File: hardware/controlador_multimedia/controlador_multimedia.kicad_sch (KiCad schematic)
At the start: 10 parts, among them J1 Conn_01x15, J2 Conn_01x15, SW1 SW_Push, SW2 SW_Push, SW3 SW_Push, SW4 RotaryEncoder_Switch

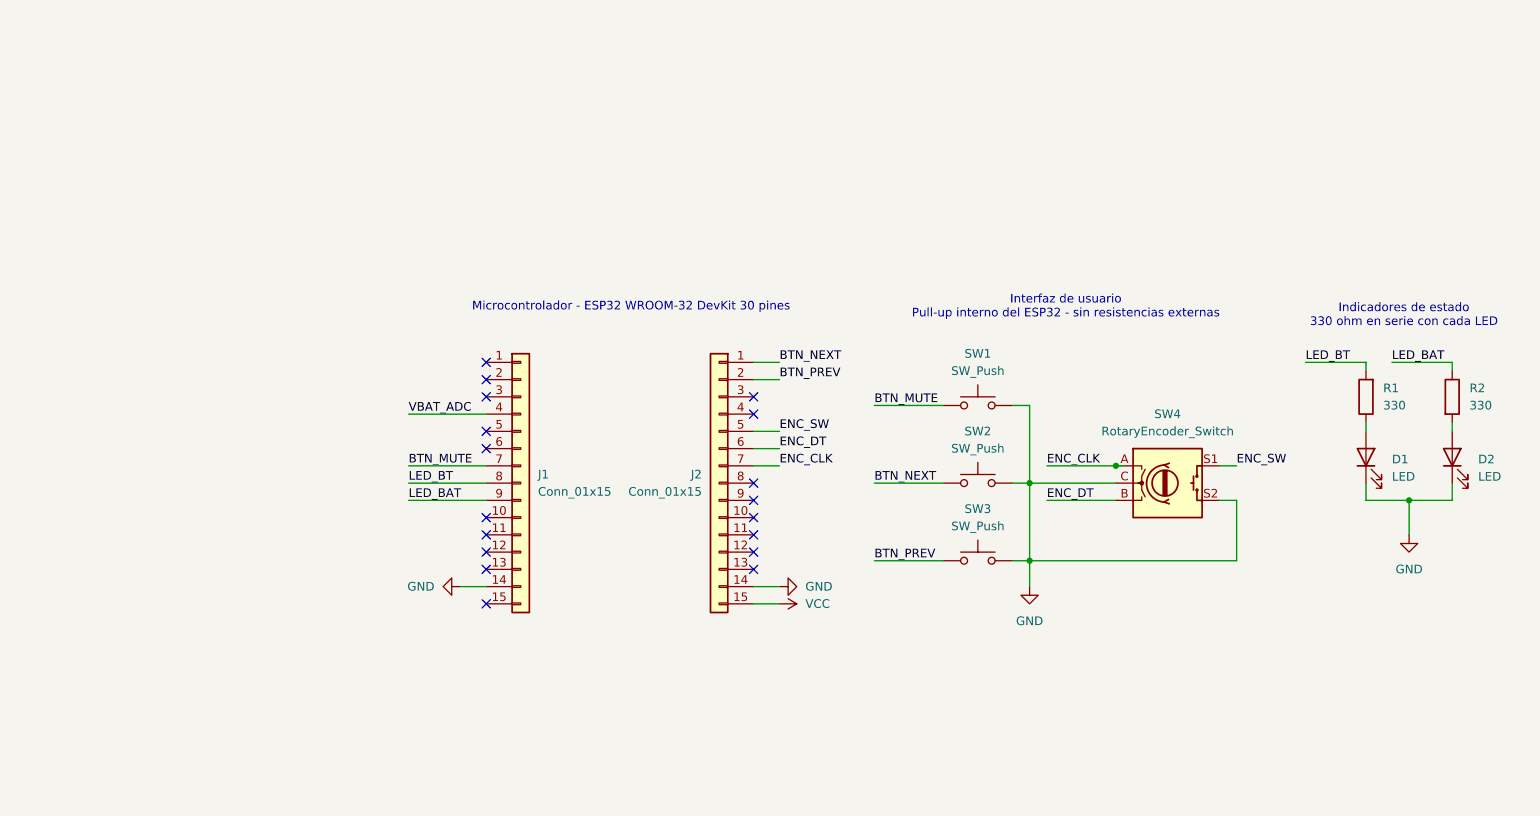
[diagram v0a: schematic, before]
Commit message: hardware: completar esquemático con cadena de potencia y ERC sin errores
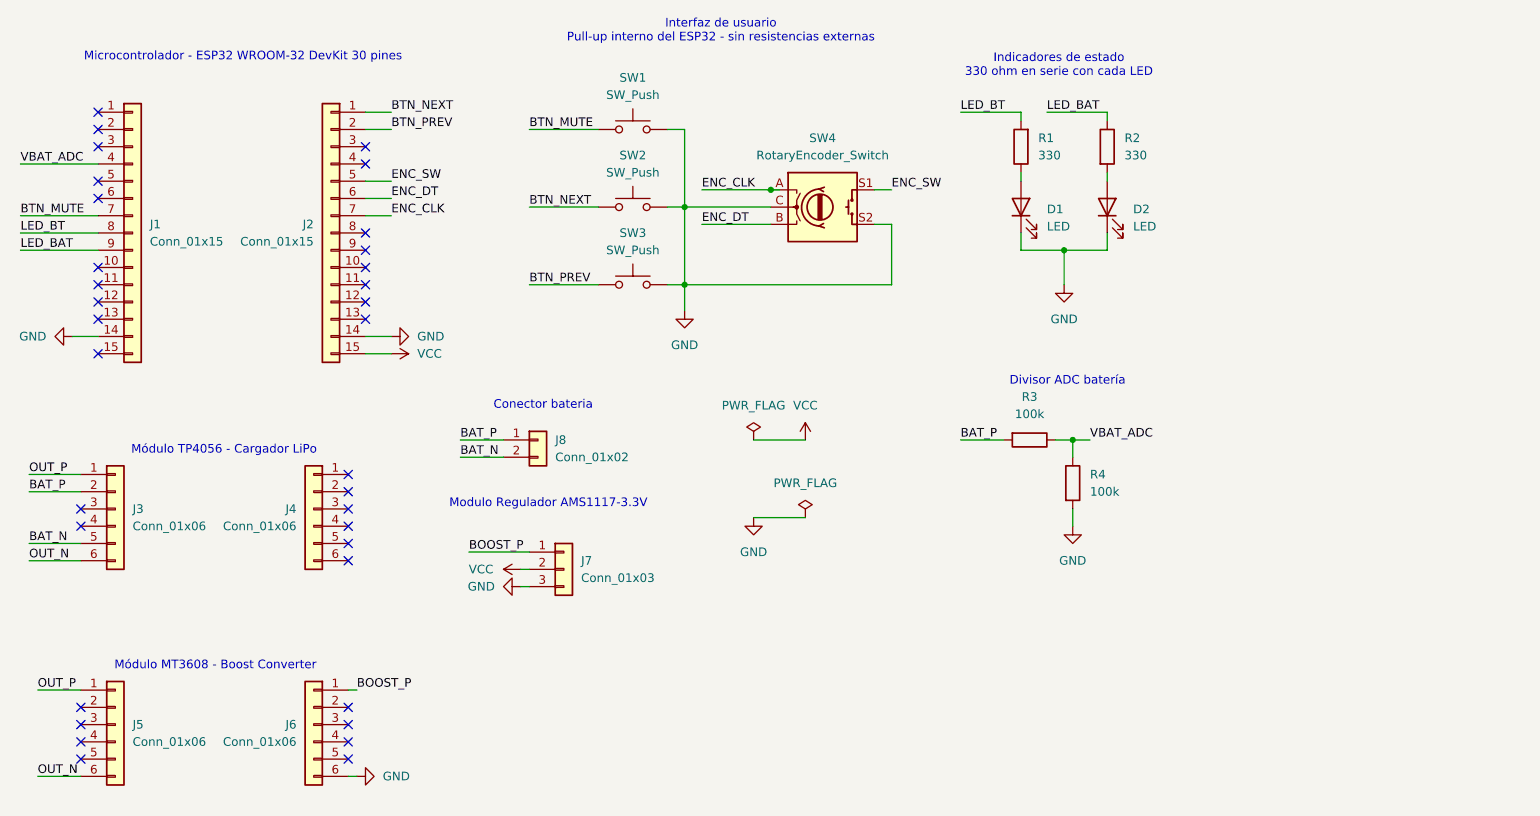
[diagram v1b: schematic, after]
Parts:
- added J3, J4, J5, J6: Conn_01x06, symbol Connector_Generic:Conn_01x06
- added J7: Conn_01x03, symbol Connector_Generic:Conn_01x03
- added J8: Conn_01x02, symbol Connector_Generic:Conn_01x02
- added R3, R4: 100k, symbol Device:R
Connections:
- net GND: now also J6.6 (Pin_6), J7.3 (Pin_3), R4.2
- net VBAT_ADC: now also R3.1, R4.1
- net VCC: now also J7.2 (Pin_2)
- new net BAT_N: J3.5 (Pin_5), J8.2 (Pin_2)
- new net BAT_P: J3.2 (Pin_2), J8.1 (Pin_1), R3.2
- new net BOOST_P: J6.1 (Pin_1), J7.1 (Pin_1)
- new net OUT_N: J3.6 (Pin_6), J5.6 (Pin_6)
- new net OUT_P: J3.1 (Pin_1), J5.1 (Pin_1)
- no-connect marks 18 -> 34
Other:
- note added: "Conector bateria"
- note added: "Divisor ADC batería"
- note added: "Modulo Regulador AMS1117-3.3V"
- note added: "Módulo MT3608 - Boost Converter"
- note added: "Módulo TP4056 - Cargador LiPo"
- company: (none) -> Mario Alberto Nina Gallo
- moved on the sheet: D1, D2, J1, J2, R1, R2, SW1, SW2, SW3, SW4

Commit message: hardware: asignar huellas y modelos 3D a todos los componentes
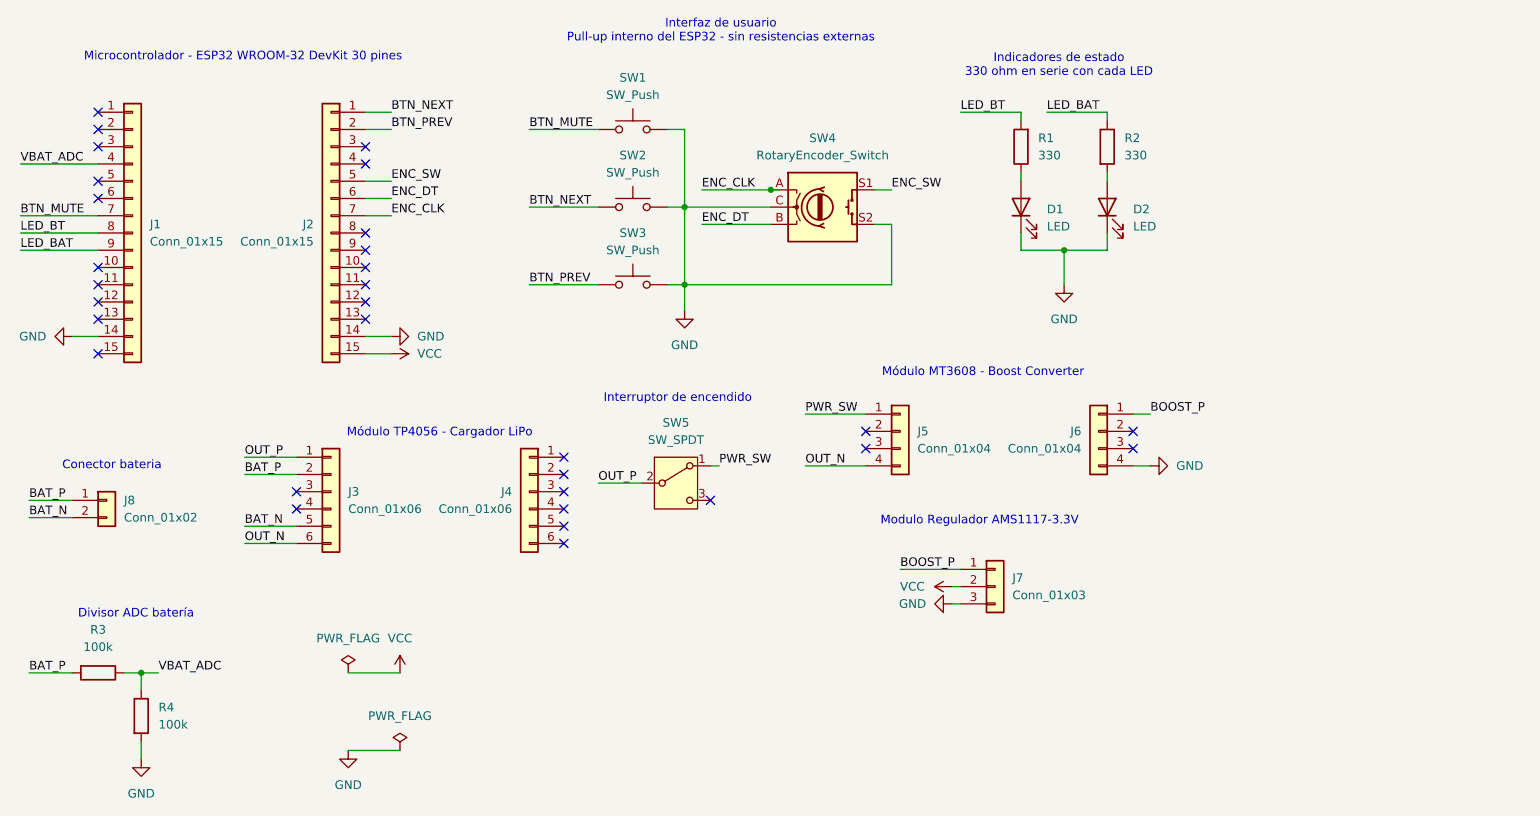
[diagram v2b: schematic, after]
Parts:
- removed J5, J6: Conn_01x06, symbol Connector_Generic:Conn_01x06
- added J5, J6: Conn_01x04, Connector_PinHeader_2.54mm:PinHeader_1x04_P2.54mm_Vertical, symbol Connector_Generic:Conn_01x04
- added SW5: SW_SPDT, Custom:Schiebeschalter_SS-12D00, symbol Switch:SW_SPDT
- D1, D2: footprint (none) -> LED_THT:LED_D5.0mm
- J1, J2: footprint (none) -> Connector_PinSocket_2.54mm:PinSocket_1x15_P2.54mm_Vertical
- J3, J4: footprint (none) -> Connector_PinHeader_2.54mm:PinHeader_1x06_P2.54mm_Vertical
- J7: footprint (none) -> Connector_PinHeader_2.54mm:PinHeader_1x03_P2.54mm_Vertical
- J8: footprint (none) -> TerminalBlock_Phoenix:TerminalBlock_Phoenix_MKDS-1,5-2_1x02_P5.00mm_Horizontal
- R1, R2, R3, R4: footprint (none) -> Resistor_THT:R_Axial_DIN0207_L6.3mm_D2.5mm_P7.62mm_Horizontal
- SW1, SW2, SW3: footprint (none) -> Button_Switch_THT:SW_PUSH_6mm_H5mm
- SW4: footprint (none) -> Rotary_Encoder:RotaryEncoder_Alps_EC11E-Switch_Vertical_H20mm
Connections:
- net BOOST_P: now also J6.1 (Pin_1)
- net GND: now also J6.4 (Pin_4)
- net OUT_N: now also J5.4 (Pin_4)
- net OUT_P: now also SW5.2 (B)
- new net PWR_SW: J5.1 (Pin_1), SW5.1 (A)
- no-connect marks 34 -> 31
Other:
- note added: "Interruptor de encendido"
- moved on the sheet: J3, J4, J7, J8, R3, R4

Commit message: refactor: centralizar pines en common/pines.h
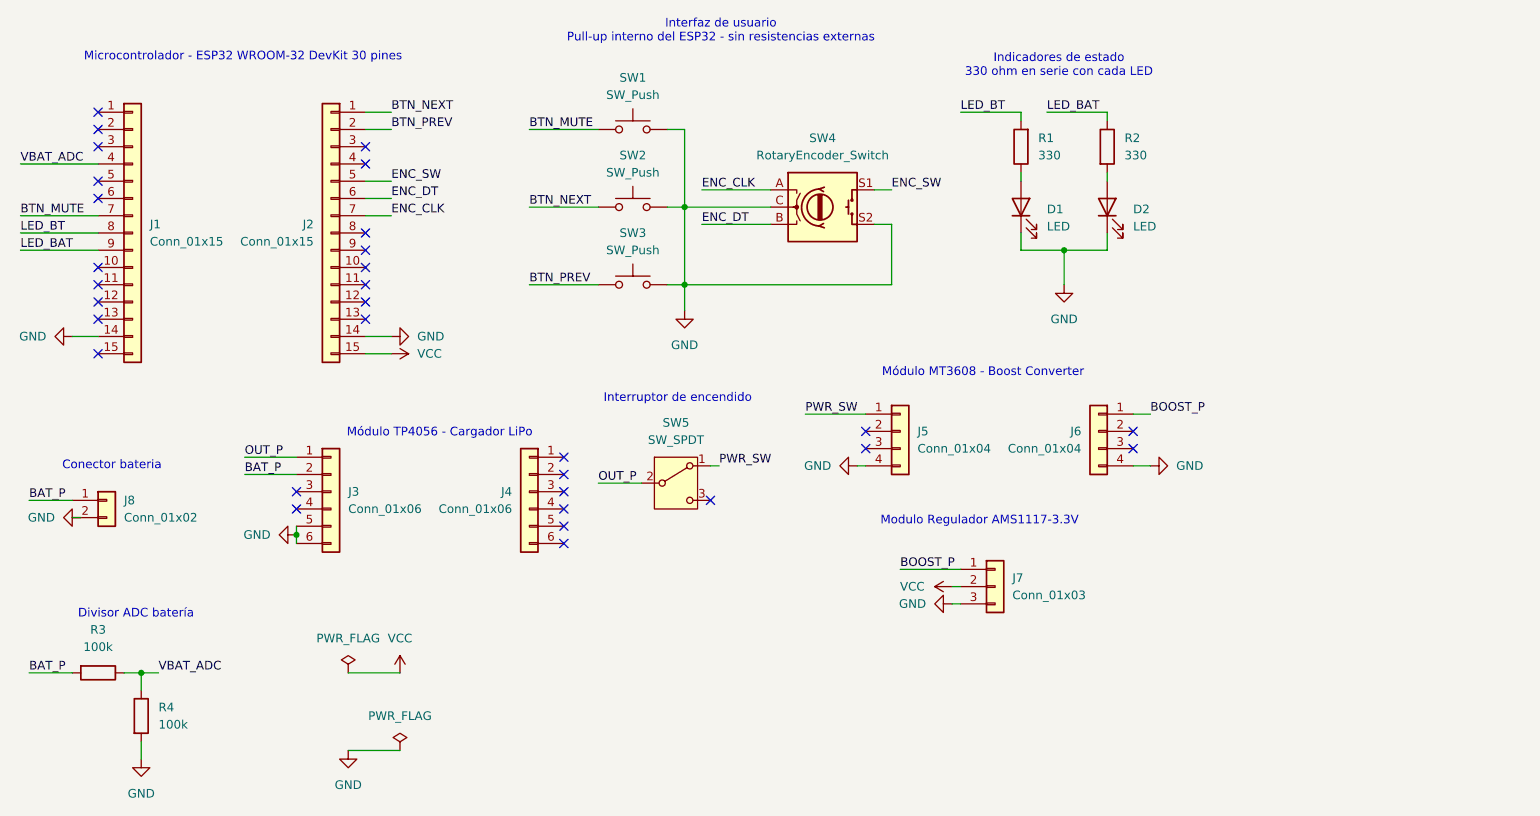
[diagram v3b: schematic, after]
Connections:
- net BAT_N is gone; now on net GND: J3.5 (Pin_5), J8.2 (Pin_2)
- net OUT_N is gone; now on net GND: J3.6 (Pin_6), J5.4 (Pin_4)
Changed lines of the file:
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@@
 	)
 	(junction
-		(at 35.56 110.49)
+		(at 58.42 90.17)
 		(diameter 0)
 		(color 0 0 0 0)
 	)
 	(junction
-		(at 128.27 39.37)
+		(at 35.56 110.49)
 		(diameter 0)
 		(color 0 0 0 0)
@@
 	(wire
 		(pts
-			(xy 50.8 88.9) (xy 58.42 88.9)
-		)
-		(stroke
-			(width 0)
-			(type default)
-		)
-	)
-	(wire
-		(pts
 			(xy 115.57 41.91) (xy 115.57 53.34)
 		)
@@
 	(wire
 		(pts
-			(xy 118.11 39.37) (xy 128.27 39.37)
-		)
-		(stroke
-			(width 0)
-			(type default)
-		)
-	)
-	(wire
-		(pts
 			(xy 156.21 27.94) (xy 165.1 27.94)
 		)
@@
 	(wire
 		(pts
+			(xy 118.11 39.37) (xy 128.27 39.37)
+		)
+		(stroke
+			(width 0)
+			(type default)
+		)
+	)
+	(wire
+		(pts
 			(xy 19.05 110.49) (xy 25.4 110.49)
 		)
@@
 	(wire
 		(pts
-			(xy 119.38 80.01) (xy 120.65 80.01)
+			(xy 58.42 90.17) (xy 58.42 91.44)
 		)
 		(stroke
@@
 	(wire
 		(pts
-			(xy 92.71 30.48) (xy 102.87 30.48)
+			(xy 119.38 80.01) (xy 120.65 80.01)
 		)
 		(stroke
@@
 	(wire
 		(pts
-			(xy 146.05 53.34) (xy 115.57 53.34)
+			(xy 92.71 30.48) (xy 102.87 30.48)
 		)
 		(stroke
@@
 	(wire
 		(pts
-			(xy 50.8 91.44) (xy 58.42 91.44)
+			(xy 146.05 53.34) (xy 115.57 53.34)
 		)
 		(stroke
@@
 	(wire
 		(pts
-			(xy 129.54 39.37) (xy 128.27 39.37)
+			(xy 115.57 30.48) (xy 115.57 41.91)
 		)
 		(stroke
@@
 	(wire
 		(pts
-			(xy 115.57 30.48) (xy 115.57 41.91)
+			(xy 140.97 80.01) (xy 142.24 80.01)
 		)
 		(stroke
@@
 	(wire
 		(pts
+			(xy 58.42 90.17) (xy 58.42 88.9)
+		)
+		(stroke
+			(width 0)
+			(type default)
+		)
+	)
+	(wire
+		(pts
 			(xy 181.61 72.39) (xy 184.15 72.39)
 		)
@@
 	(wire
 		(pts
-			(xy 133.35 80.01) (xy 142.24 80.01)
+			(xy 26.67 87.63) (xy 25.4 87.63)
 		)
 		(stroke
@@
 	(wire
 		(pts
-			(xy 19.05 87.63) (xy 25.4 87.63)
-		)
-		(stroke
-			(width 0)
-			(type default)
-		)
-	)
-	(wire
-		(pts
 			(xy 115.57 53.34) (xy 115.57 57.15)
 		)
@@
 		)
 	)
-	(label "BAT_N"
-		(at 19.05 87.63 0)
-		(effects
-			(font
-				(size 1.27 1.27)
-			)
-			(justify left bottom)
-		)
-	)
 	(label "BAT_P"
 		(at 50.8 81.28 0)
@@
 		)
 	)
-	(label "BAT_N"
-		(at 50.8 88.9 0)
-		(effects
-			(font
-				(size 1.27 1.27)
-			)
-			(justify left bottom)
-		)
-	)
 	(label "ENC_DT"
 		(at 118.11 44.45 0)
@@
 		)
 	)
-	(label "OUT_N"
-		(at 50.8 91.44 0)
-		(effects
-			(font
-				(size 1.27 1.27)
-			)
-			(justify left bottom)
-		)
-	)
 	(label "LED_BAT"
 		(at 168.91 27.94 0)
@@
 		)
 	)
-	(label "OUT_N"
-		(at 133.35 80.01 0)
-		(effects
-			(font
-				(size 1.27 1.27)
-			)
-			(justify left bottom)
-		)
-	)
 	(label "ENC_CLK"
 		(at 72.39 43.18 0)
@@
 	)
 	(symbol
+		(lib_id "power:GND")
+		(at 26.67 87.63 270)
+		(unit 1)
+		(exclude_from_sim no)
+		(in_bom yes)
+		(on_board yes)
+		(dnp no)
+		(fields_autoplaced yes)
+		(property "Reference" "#PWR12"
+			(at 20.32 87.63 0)
+			(effects
+				(font
+					(size 1.27 1.27)
+				)
+				(hide yes)
+			)
+		)
+		(property "Value" "GND"
+			(at 22.86 87.6299 90)
+			(effects
+				(font
+					(size 1.27 1.27)
+				)
+				(justify right)
+			)
+		)
+		(property "Footprint" ""
+			(at 26.67 87.63 0)
+			(effects
+				(font
+					(size 1.27 1.27)
+				)
+				(hide yes)
+			)
+		)
+		(property "Datasheet" ""
+			(at 26.67 87.63 0)
+			(effects
+				(font
+					(size 1.27 1.27)
+				)
+				(hide yes)
+			)
+		)
+		(property "Description" "Power symbol creates a global label with name \"GND\" , ground"
+			(at 26.67 87.63 0)
+			(effects
+				(font
+					(size 1.27 1.27)
+				)
+				(hide yes)
+			)
+		)
+		(pin "1"
+		)
+		(instances
+			(project ""
+				(path "/0b82bd40-e028-45e2-90c6-3c47a134a0e6"
+					(reference "#PWR12")
+					(unit 1)
+				)
+			)
+		)
+	)
+	(symbol
 		(lib_id "Switch:SW_SPDT")
 		(at 114.3 82.55 0)
@@
 	)
 	(symbol
+		(lib_id "power:GND")
+		(at 140.97 80.01 270)
+		(unit 1)
+		(exclude_from_sim no)
+		(in_bom yes)
+		(on_board yes)
+		(dnp no)
+		(fields_autoplaced yes)
+		(property "Reference" "#PWR14"
+			(at 134.62 80.01 0)
+			(effects
+				(font
+					(size 1.27 1.27)
+				)
+				(hide yes)
+			)
+		)
+		(property "Value" "GND"
+			(at 137.16 80.0099 90)
+			(effects
+				(font
+					(size 1.27 1.27)
+				)
+				(justify right)
+			)
+		)
+		(property "Footprint" ""
+			(at 140.97 80.01 0)
+			(effects
+				(font
+					(size 1.27 1.27)
+				)
+				(hide yes)
+			)
+		)
+		(property "Datasheet" ""
+			(at 140.97 80.01 0)
+			(effects
+				(font
+					(size 1.27 1.27)
+				)
+				(hide yes)
+			)
+		)
+		(property "Description" "Power symbol creates a global label with name \"GND\" , ground"
+			(at 140.97 80.01 0)
+			(effects
+				(font
+					(size 1.27 1.27)
+				)
+				(hide yes)
+			)
+		)
+		(pin "1"
+		)
+		(instances
+			(project ""
+				(path "/0b82bd40-e028-45e2-90c6-3c47a134a0e6"
+					(reference "#PWR14")
+					(unit 1)
+				)
+			)
+		)
+	)
+	(symbol
 		(lib_id "power:VCC")
 		(at 154.94 97.79 90)
@@
 					(unit 1)
 				)
+			)
+		)
+	)
+	(symbol
+		(lib_id "power:GND")
+		(at 58.42 90.17 270)
+		(unit 1)
+		(exclude_from_sim no)
+		(in_bom yes)
+		(on_board yes)
+		(dnp no)
+		(fields_autoplaced yes)
+		(property "Reference" "#PWR13"
+			(at 52.07 90.17 0)
+			(effects
+				(font
+					(size 1.27 1.27)
+				)
+				(hide yes)
+			)
+		)
+		(property "Value" "GND"
+			(at 54.61 90.1699 90)
+			(effects
+				(font
+					(size 1.27 1.27)
+				)
+				(justify right)
+			)
+		)
+		(property "Footprint" ""
+			(at 58.42 90.17 0)
+			(effects
+				(font
+					(size 1.27 1.27)
+				)
+				(hide yes)
+			)
+		)
+		(property "Datasheet" ""
+			(at 58.42 90.17 0)
+			(effects
+				(font
+					(size 1.27 1.27)
+				)
+				(hide yes)
+			)
+		)
+		(property "Description" "Power symbol creates a global label with name \"GND\" , ground"
+			(at 58.42 90.17 0)
+			(effects
+				(font
+					(size 1.27 1.27)
+				)
+				(hide yes)
+			)
+		)
+		(pin "1"
+		)
+		(instances
+			(project ""
+				(path "/0b82bd40-e028-45e2-90c6-3c47a134a0e6"
+					(reference "#PWR13")
+					(unit 1)
+				)
